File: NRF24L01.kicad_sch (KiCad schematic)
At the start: 19 parts, among them J3 Conn_Coaxial, U3 NRF24L01, Y2 16MHz

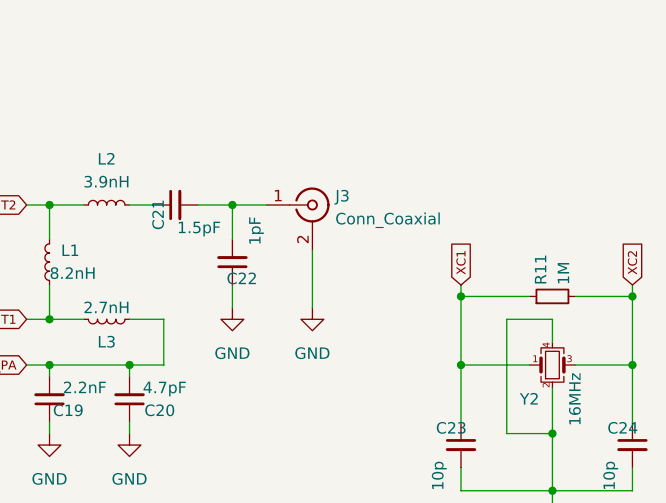
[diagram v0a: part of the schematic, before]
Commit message: removed sma connector -> wrong footprint
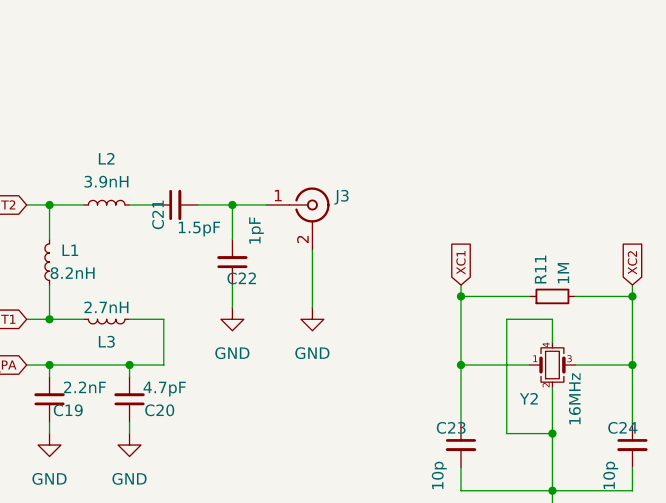
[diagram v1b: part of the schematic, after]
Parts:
- J3: value Conn_Coaxial -> (none); footprint Connector_Coaxial:SMA_Amphenol_132289_EdgeMount -> (none)
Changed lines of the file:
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@@
       (effects (font (size 1.27 1.27)) (justify left))
     )
-    (property "Value" "Conn_Coaxial" (id 1) (at 196.85 77.7631 0)
+    (property "Value" "" (id 1) (at 196.85 77.7631 0)
       (effects (font (size 1.27 1.27)) (justify left))
     )
-    (property "Footprint" "Connector_Coaxial:SMA_Amphenol_132289_EdgeMount" (id 2) (at 194.31 76.2 0)
+    (property "Footprint" "" (id 2) (at 194.31 76.2 0)
       (effects (font (size 1.27 1.27)) hide)
     )

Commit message: updated pictures
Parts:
- J3: value (none) -> Conn_Coaxial; footprint (none) -> Connector_Coaxial:SMA_Samtec_SMA-J-P-X-ST-EM1_EdgeMount
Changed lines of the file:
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@@
       (effects (font (size 1.27 1.27)) (justify left))
     )
-    (property "Value" "" (id 1) (at 196.85 77.7631 0)
+    (property "Value" "Conn_Coaxial" (id 1) (at 196.85 77.7631 0)
       (effects (font (size 1.27 1.27)) (justify left))
     )
-    (property "Footprint" "" (id 2) (at 194.31 76.2 0)
+    (property "Footprint" "Connector_Coaxial:SMA_Samtec_SMA-J-P-X-ST-EM1_EdgeMount" (id 2) (at 194.31 76.2 0)
       (effects (font (size 1.27 1.27)) hide)
     )
